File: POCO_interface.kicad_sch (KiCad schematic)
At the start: 2 parts, among them J1 Conn_02x25_Odd_Even, J2 N10280-52E2PC

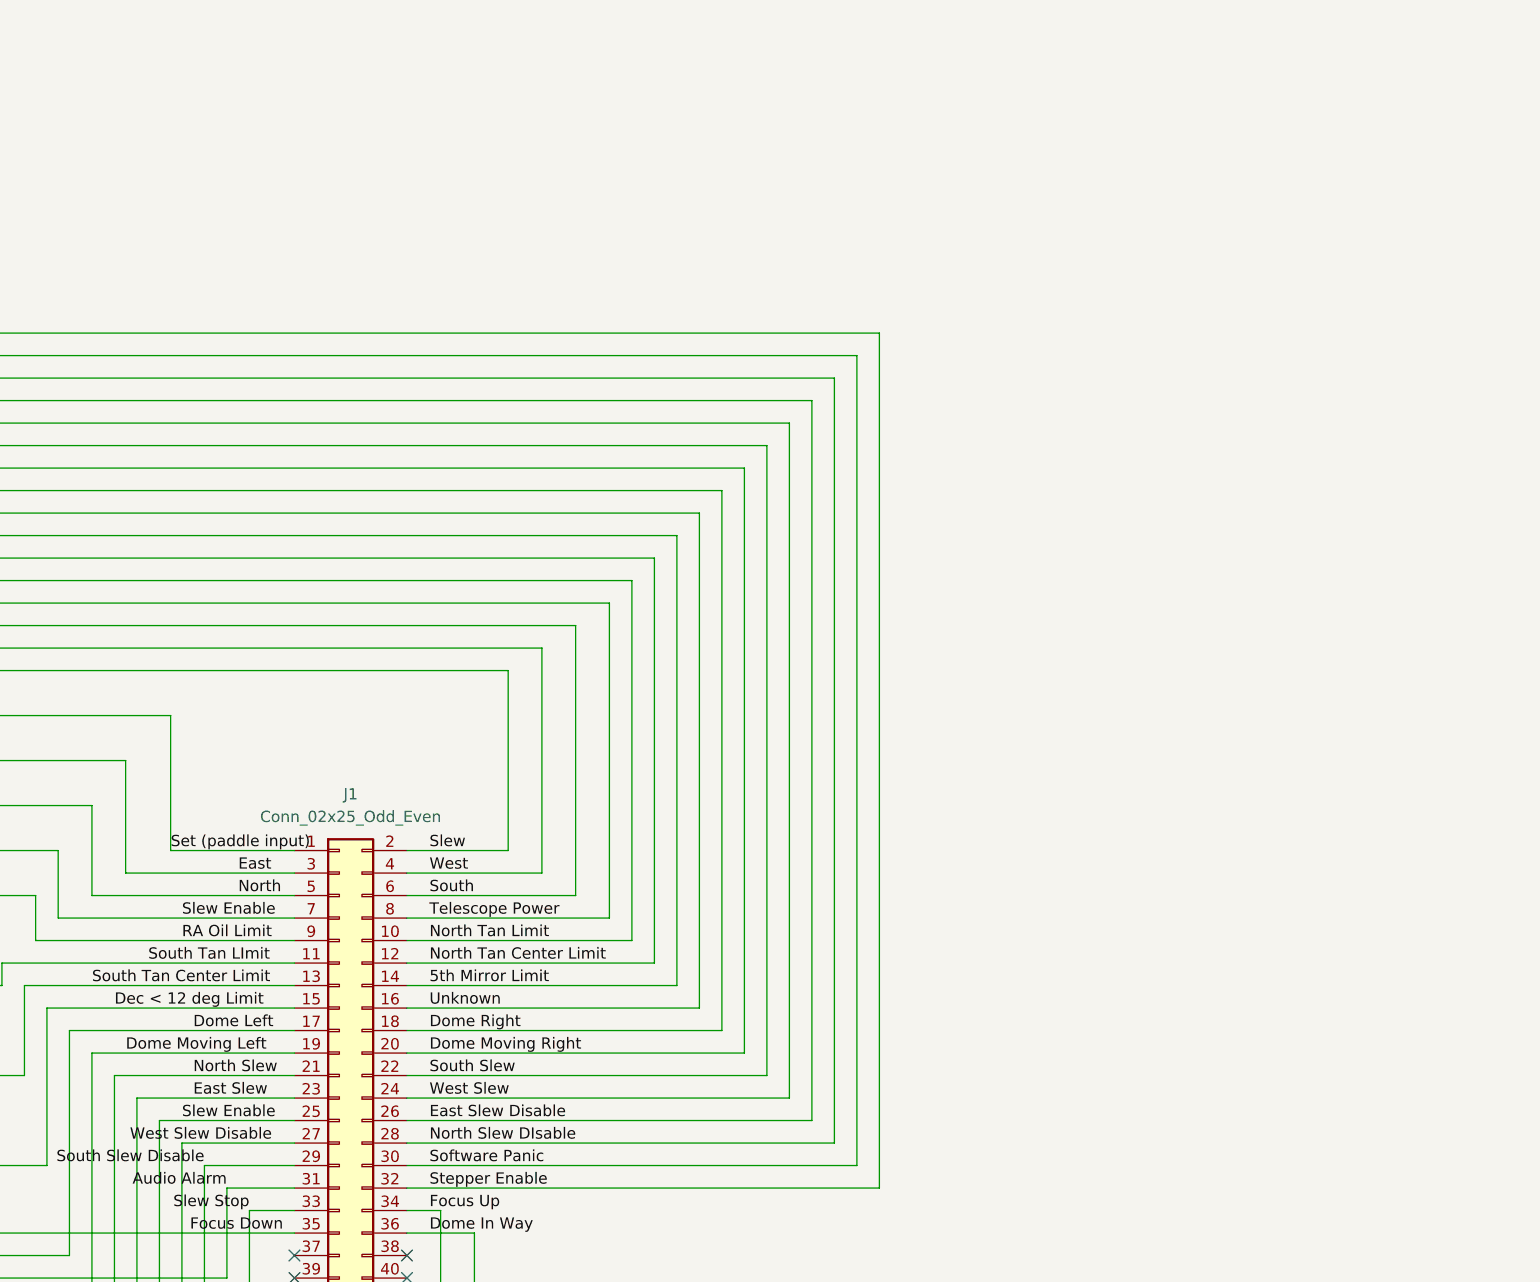
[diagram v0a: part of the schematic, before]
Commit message: Completed PCB layout
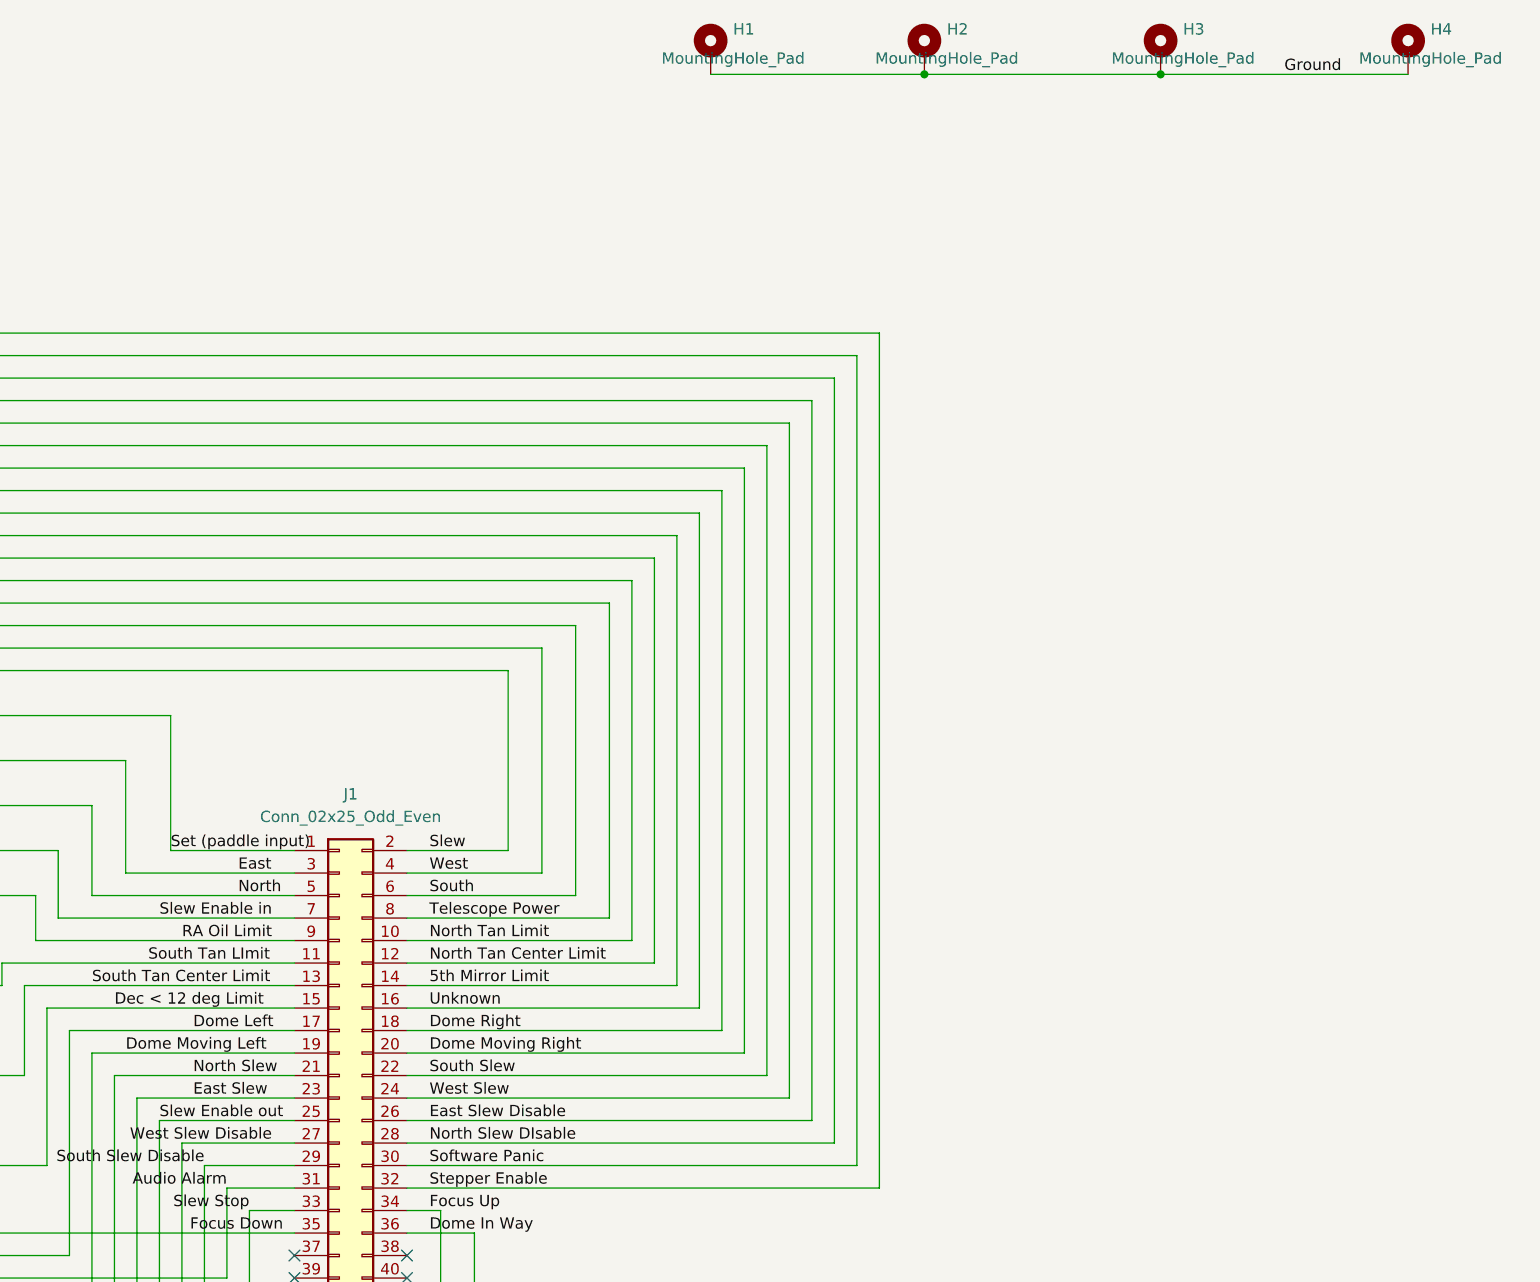
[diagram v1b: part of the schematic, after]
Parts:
- added H1, H2, H3, H4: MountingHole_Pad, MountingHole:MountingHole_3.2mm_M3_DIN965_Pad, symbol Mechanical:MountingHole_Pad
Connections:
- net Ground: now also H1.1, H2.1, H3.1, H4.1
- net Slew Enable renamed Slew Enable in
- net Slew Enable in: no longer J1.25 (Pin_25), J2.42
- new net Slew Enable out: J1.25 (Pin_25), J2.42
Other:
- title: (none) -> POCO: Galil Extended IO to Digital IO Interface PCB
